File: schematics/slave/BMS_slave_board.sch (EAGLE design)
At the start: 58 parts, among them IC1 ATTINY87/167AUTOMOTIVESOIC, IC2 LT1021S, IC3 78L05F, J1 AVR_SPI_PRG_6NS, Q1 BSS123, Q2 BSS123, Q3 BSS123, Q4 BSS123, U1 LMV324, U2 LMV324, X1 87438-05, X2 87438-05

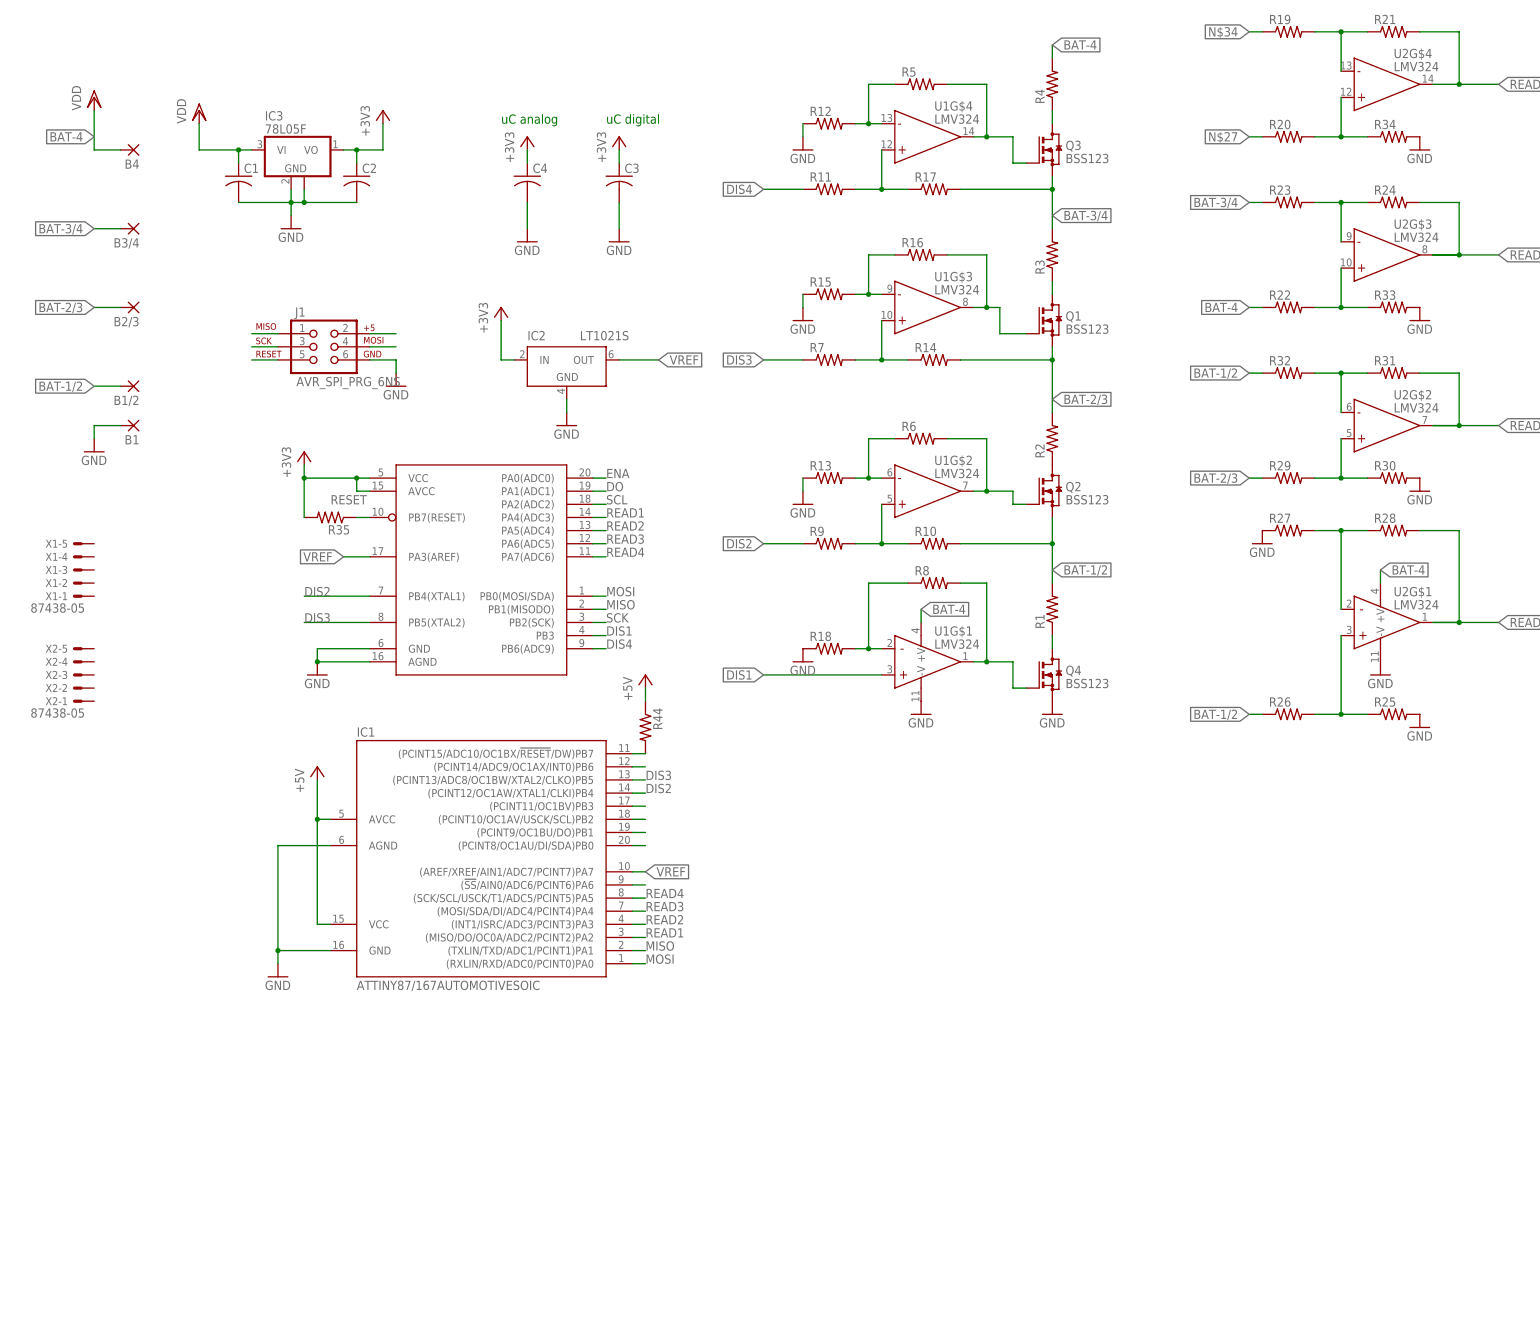
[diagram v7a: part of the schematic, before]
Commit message: added new optos, moved around pins as necessary and added LIN Driver
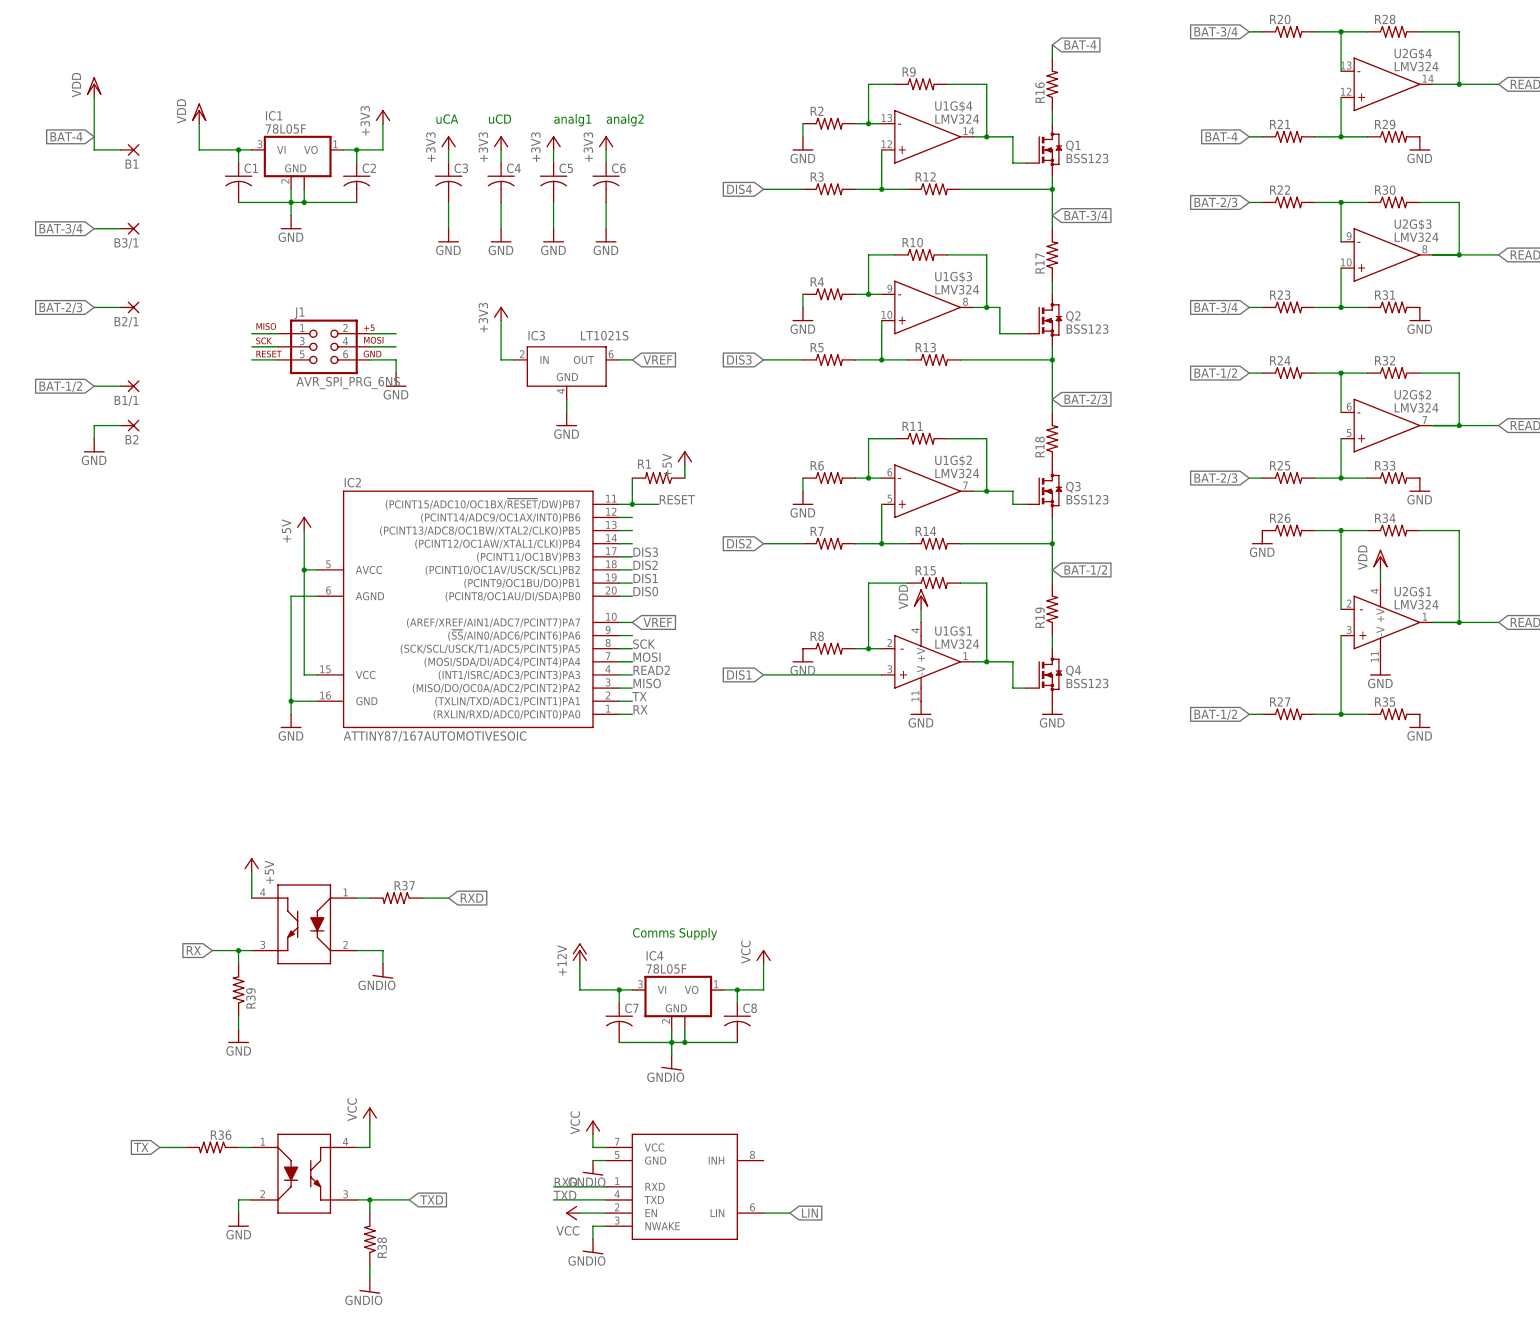
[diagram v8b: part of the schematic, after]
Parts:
- removed B4: (no value), wirepad:2,15/1,0
- removed R44: (no value), rcl:R-US_R0603
- removed X1, X2: 87438-05, con-molex:87438-05
- added B2: (no value), wirepad:2,15/1,0
- added C5, C6, C7, C8: (no value), resistor:C-US025-024X044
- added IC4: 78L05F, linear:78L05F
- added R36, R37, R38, R39: (no value), rcl:R-US_R0603
- added U$2: LTV-817, EVT-Eagle-Library:LTV-817
- added U$3: TPIC1021, EVT-Eagle-Library:TPIC1021
- IC1: value ATTINY87/167AUTOMOTIVESOIC -> 78L05F; device EVT-Eagle-Library:ATTINY87/167AUTOMOTIVESOIC -> linear:78L05F
- IC2: value LT1021S -> ATTINY87/167AUTOMOTIVESOIC; device linear-technology:LT1021S -> EVT-Eagle-Library:ATTINY87/167AUTOMOTIVESOIC
- IC3: value 78L05F -> LT1021S; device linear:78L05F -> linear-technology:LT1021S
- R19: device rcl:R-US_M0805 -> rcl:R-US_R0603
- R20: device rcl:R-US_R0603 -> rcl:R-US_M0805
- U$1: value ATTINY261ASOC -> LTV-817; device EVT-Eagle-Library:ATTINY261ASOC -> EVT-Eagle-Library:LTV-817
- renumbered B1/2 to B1/1, B2/3 to B2/1, B3/4 to B3/1
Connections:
- removed net DO: U$1.PA1(ADC1)
- removed net ENA: U$1.PA0(ADC0)
- removed net N$32: IC1.(PCINT11/OC1BV)PB3
- removed net N$34: R19.1
- removed net N$35: IC1.(PCINT10/OC1AV/USCK/SCL)PB2
- removed net N$36: IC1.(PCINT9/OC1BU/DO)PB1
- removed net N$37: IC1.(PCINT8/OC1AU/DI/SDA)PB0
- removed net SCL: U$1.PA2(ADC2)
- new net +12V: C7.1, IC4.VI
- new net DIS0: IC2.(PCINT8/OC1AU/DI/SDA)PB0
- new net GNDIO: C7.2, C8.2, IC4.GND, IC4.GND@1, R38.1, U$1.CA, U$3.GND, U$3.NWAKE
- new net LIN: U$3.LIN
- new net N$23: IC2.(PCINT13/ADC8/OC1BW/XTAL2/CLKO)PB5
- new net N$29: R37.2, U$1.A
- new net RX: IC2.(RXLIN/RXD/ADC0/PCINT0)PA0, R39.2, U$1.E
- new net RXD: R37.1, U$3.RXD
- new net TX: IC2.(TXLIN/TXD/ADC1/PCINT1)PA1, R36.2
- new net TXD: R38.2, U$2.E, U$3.TXD
- new net VCC: C8.1, IC4.VO, U$2.CO, U$3.EN, U$3.VCC
- net +3V3: now also C5.1, C6.1, IC1.VO, IC3.IN; no longer IC2.IN, IC3.VO, R35.2, U$1.AVCC, U$1.VCC
- net +5V: now also IC2.AVCC, IC2.VCC, R1.1, U$1.CO; no longer IC1.AVCC, IC1.VCC, R44.1
- net BAT-1/2: now also Q3.S, R14.2, R19.2, R24.1, R27.1; no longer Q2.S, R1.2, R10.2, R26.1, R32.1
- net BAT-2/3: now also Q2.S, R13.2, R18.2, R22.1, R25.1; no longer Q1.S, R14.2, R2.2, R29.1
- net BAT-3/4: now also Q1.S, R12.2, R20.1; no longer Q3.S, R3.2
- net BAT-4: now also B1.P, R16.2, R21.1; no longer B4.P, R22.1, R4.2, U1G$1.+V, U2G$1.+V
- net DELDEL: now also R10.1, R4.2; no longer R15.2, R16.1
- net DIS1: now also IC2.(PCINT9/OC1BU/DO)PB1; no longer U$1.PB3
- net DIS2: now also IC2.(PCINT10/OC1AV/USCK/SCL)PB2, R7.1; no longer IC1.(PCINT12/OC1AW/XTAL1/CLKI)PB4, R9.1, U$1.PB4(XTAL1)
- net DIS3: now also IC2.(PCINT11/OC1BV)PB3, R5.1; no longer IC1.(PCINT13/ADC8/OC1BW/XTAL2/CLKO)PB5, R7.1, U$1.PB5(XTAL2)
- net DIS4: now also R3.1; no longer R11.1, U$1.PB6(ADC9)
- net GND: now also B2.P, C5.2, C6.2, IC1.GND@1, IC2.AGND, R2.1, R26.1, R29.2, R31.2, R35.2, R39.1, R4.1, R6.1, R8.1, U$2.CA; no longer B1.P, IC1.AGND, IC3.GND@1, R12.1, R13.1, R15.1, R18.1, R25.2, R27.1, R30.2, R34.2, U$1.AGND, U$1.GND
- net MISO: now also IC2.(MISO/DO/OC0A/ADC2/PCINT2)PA2; no longer IC1.(TXLIN/TXD/ADC1/PCINT1)PA1, U$1.PB1(MISODO)
- net MOSI: now also IC2.(MOSI/SDA/DI/ADC4/PCINT4)PA4; no longer IC1.(RXLIN/RXD/ADC0/PCINT0)PA0, U$1.PB0(MOSI/SDA)
- net N$1: now also Q2.D, R17.1; no longer Q1.D, R3.1
- net N$10: now also R14.1, R7.2; no longer R10.1, R9.2
- net N$11: now also R20.2, R28.1; no longer R19.2, R21.1
- net N$12: now also R11.1, R6.2; no longer R13.2, R6.1
- net N$13: now also R22.2, R30.1; no longer R23.2, R24.1
- net N$14: now also R2.2, R9.1; no longer R12.2, R5.1
- net N$15: now also R12.1, R3.2; no longer R11.2, R17.1
- net N$16: now also R21.2, R29.1; no longer R20.2, R34.1
- net N$17: now also R23.2, R31.1; no longer R22.2, R33.1
- net N$18: now also R25.2, R33.1; no longer R29.2, R30.1
- net N$19: now also R27.2, R35.1; no longer R25.1, R26.2
- net N$2: now also R13.1, R5.2; no longer R14.1, R7.2
- net N$20: now also R24.2, R32.1; no longer R31.1, R32.2
- net N$21: now also IC2.(PCINT12/OC1AW/XTAL1/CLKI)PB4; no longer IC1.(PCINT15/ADC10/OC1BX/!RESET!/DW)PB7, R44.2
- net N$22: now also R26.2, R34.1; no longer R27.2, R28.1
- net N$24: now also IC2.(PCINT14/ADC9/OC1AX/INT0)PB6; no longer IC1.(PCINT14/ADC9/OC1AX/INT0)PB6
- net N$27: now also R36.1, U$2.A; no longer R20.1
- net N$3: now also Q3.D, R18.1; no longer Q2.D, R2.1
- net N$33: now also Q1.G, R9.2; no longer Q3.G, R5.2
- net N$39: now also IC2.(!SS!/AIN0/ADC6/PCINT6)PA6; no longer IC1.(!SS!/AIN0/ADC6/PCINT6)PA6
- net N$4: now also R15.1, R8.2; no longer R18.2, R8.1
- net N$5: now also Q1.D, R16.1; no longer Q3.D, R4.1
- net N$6: now also Q3.G, R11.2; no longer Q2.G, R6.2
- net N$7: now also R19.1; no longer R1.1
- net N$8: now also R15.2; no longer R8.2
- net N$9: now also Q2.G, R10.2; no longer Q1.G, R16.2
- net READ1: now also R34.2; no longer IC1.(MISO/DO/OC0A/ADC2/PCINT2)PA2, R28.2, U$1.PA4(ADC3)
- net READ2: now also IC2.(INT1/ISRC/ADC3/PCINT3)PA3, R32.2; no longer IC1.(INT1/ISRC/ADC3/PCINT3)PA3, R31.2, U$1.PA5(ADC4)
- net READ3: now also R30.2; no longer IC1.(MOSI/SDA/DI/ADC4/PCINT4)PA4, R24.2, U$1.PA6(ADC5)
- net READ4: now also R28.2; no longer IC1.(SCK/SCL/USCK/T1/ADC5/PCINT5)PA5, R21.2, U$1.PA7(ADC6)
- net RESET: now also IC2.(PCINT15/ADC10/OC1BX/!RESET!/DW)PB7, R1.2; no longer R35.1, U$1.PB7(RESET)
- net SCK: now also IC2.(SCK/SCL/USCK/T1/ADC5/PCINT5)PA5; no longer U$1.PB2(SCK)
- net VDD: now also IC1.VI, U1G$1.+V, U2G$1.+V; no longer IC3.VI
- net VREF: now also IC2.(AREF/XREF/AIN1/ADC7/PCINT7)PA7, IC3.OUT; no longer IC1.(AREF/XREF/AIN1/ADC7/PCINT7)PA7, IC2.OUT, U$1.PA3(AREF)
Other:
- note added: "Comms Supply"
- note added: "analg1"
- note added: "analg2"
- note added: "uCA"
- note added: "uCD"
- note removed: "uC analog"
- note removed: "uC digital"
- moved on the sheet: B1, C3, C4, Q1, Q2, Q3, R1, R10, R11, R12, R13, R14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
